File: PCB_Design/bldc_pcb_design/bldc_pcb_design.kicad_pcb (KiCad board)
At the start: 4 copper layers, 55.5 x 55.5 mm, 79 parts, among them IC1 DRV8305NPHPR, J1 Conn_01x06_Female, SW1 BOOT, SW2 RESET, U1 ESP32-WROOM-32D, U10 DS18S20Z+, U2 AS5600-ASOT, U3 LM2672M-3.3, U4 CSD18532NQ5BT, U5 CSD18532NQ5BT, U6 CSD18532NQ5BT, U7 CSD18532NQ5BT, U8 CSD18532NQ5BT, U9 CSD18532NQ5BT

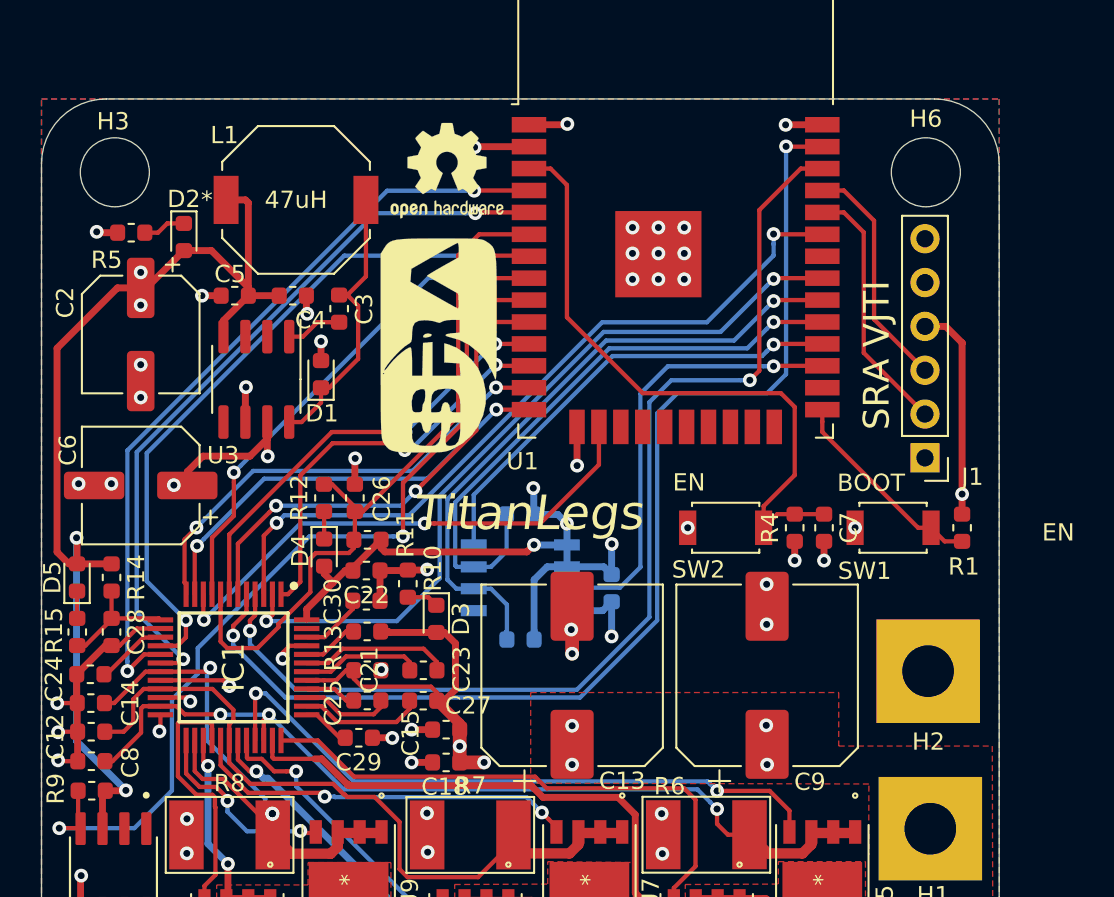
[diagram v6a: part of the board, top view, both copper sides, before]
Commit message: Routed buck converter LM2672 by copper fills - FCu
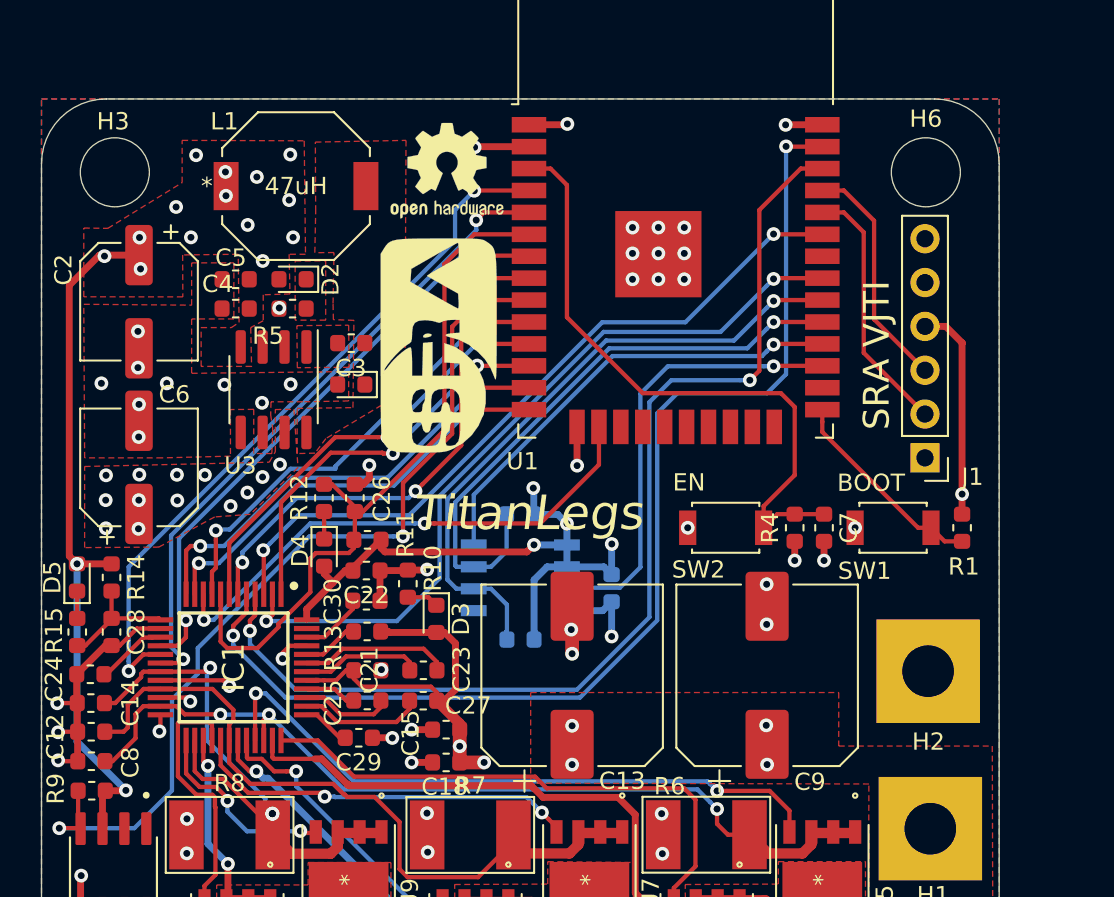
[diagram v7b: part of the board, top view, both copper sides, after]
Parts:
- moved R5 10.3 mm to (80.3, 73.9)
- moved D2 6.76 mm to (80.3, 72.2), turned to 180 degrees
- moved REF** 4.63 mm to (103.0, 104.5)
- moved C4 3.40 mm to (77.0, 73.9), turned to 180 degrees
- moved C3 2.12 mm to (83.7, 75.9), turned to 0 degrees
- moved C2 1.90 mm to (71.4, 73.5)
- moved D1 1.85 mm to (83.7, 78.3), turned to 180 degrees
- moved U3 1.17 mm to (79.2, 78.6)
- moved C6 1.05 mm to (71.4, 83.1), turned to 90 degrees
- moved C5 0.95 mm to (77.0, 72.2)
- moved L1 0.80 mm to (80.5, 66.8)
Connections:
- IC1 pad 17: ISENB -> POWER_IN
- U1 pad 4: ISENB -> POWER_IN
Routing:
- net ISENB: track 44.6 -> 0.00 mm, vias 2 -> 0
- net POWER_IN: track 54.2 -> 86.7 mm, vias 23 -> 36
- net 3V3_IN: track 114.9 -> 93.4 mm, vias 11 -> 23
- net Net-(C3-Pad2): track 16.4 -> 0.00 mm
- net GND: track 57.0 -> 50.7 mm, vias 55 -> 56
- net ISENA: track 40.2 -> 34.7 mm
- net ISENC: track 43.0 -> 37.7 mm
- net Net-(C3-Pad1): track 3.24 -> 0.00 mm
- net Net-(D2-Pad1): track 2.49 -> 0.00 mm
- net DRV_LA: track 43.7 -> 42.6 mm
- net DRV_EN_GATE: track 23.8 -> 23.1 mm
- net DRV_SPI_MISO: track 25.4 -> 24.7 mm
- net DRV_SPI_CLK: track 26.8 -> 26.3 mm
- added copper zone on F.Cu, net 3V3_IN
- added copper zone on F.Cu, net GND
- added copper zone on F.Cu, net Net-(C3-Pad1)
- added copper zone on F.Cu, net Net-(C3-Pad2)
- added copper zone on F.Cu, net Net-(D2-Pad1)

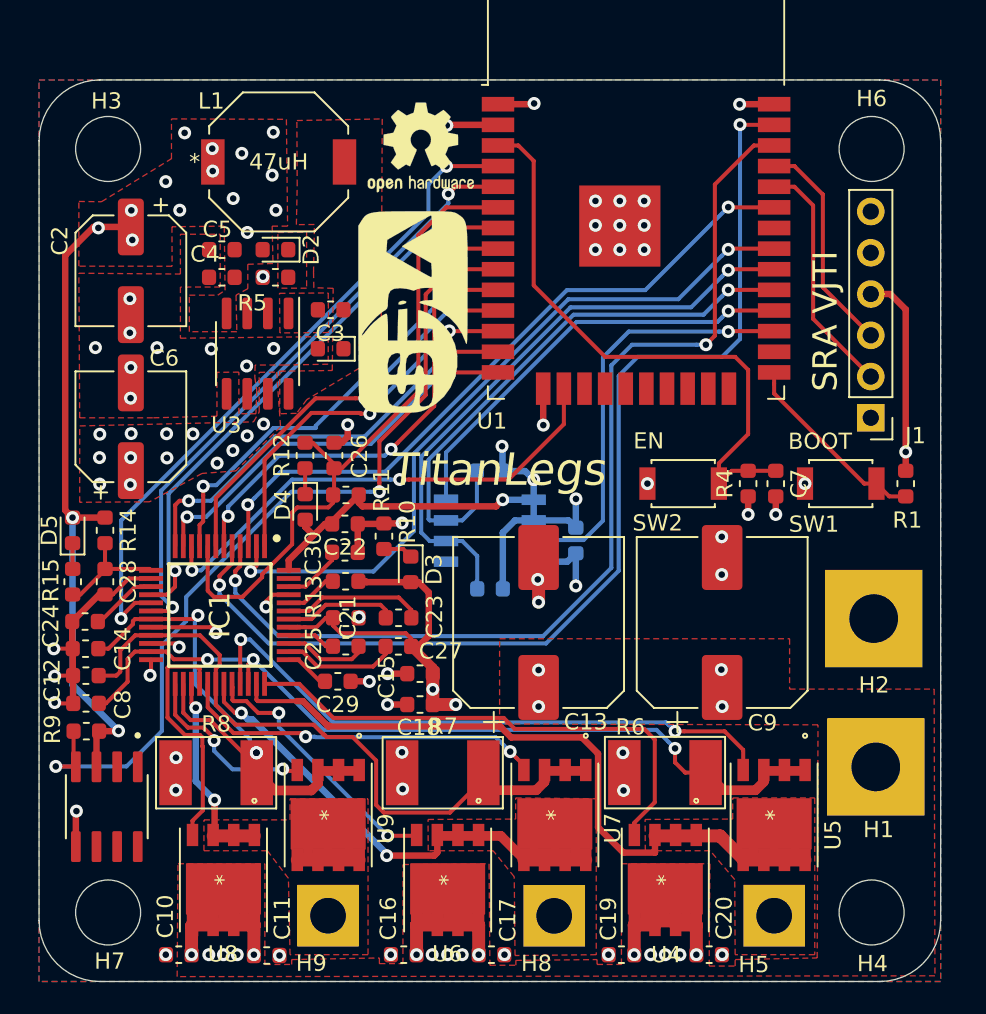
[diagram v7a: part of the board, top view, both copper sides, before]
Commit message: Re-routed DRV8305 using corrected underneath GND pad footprint, back mounted Temp sensor
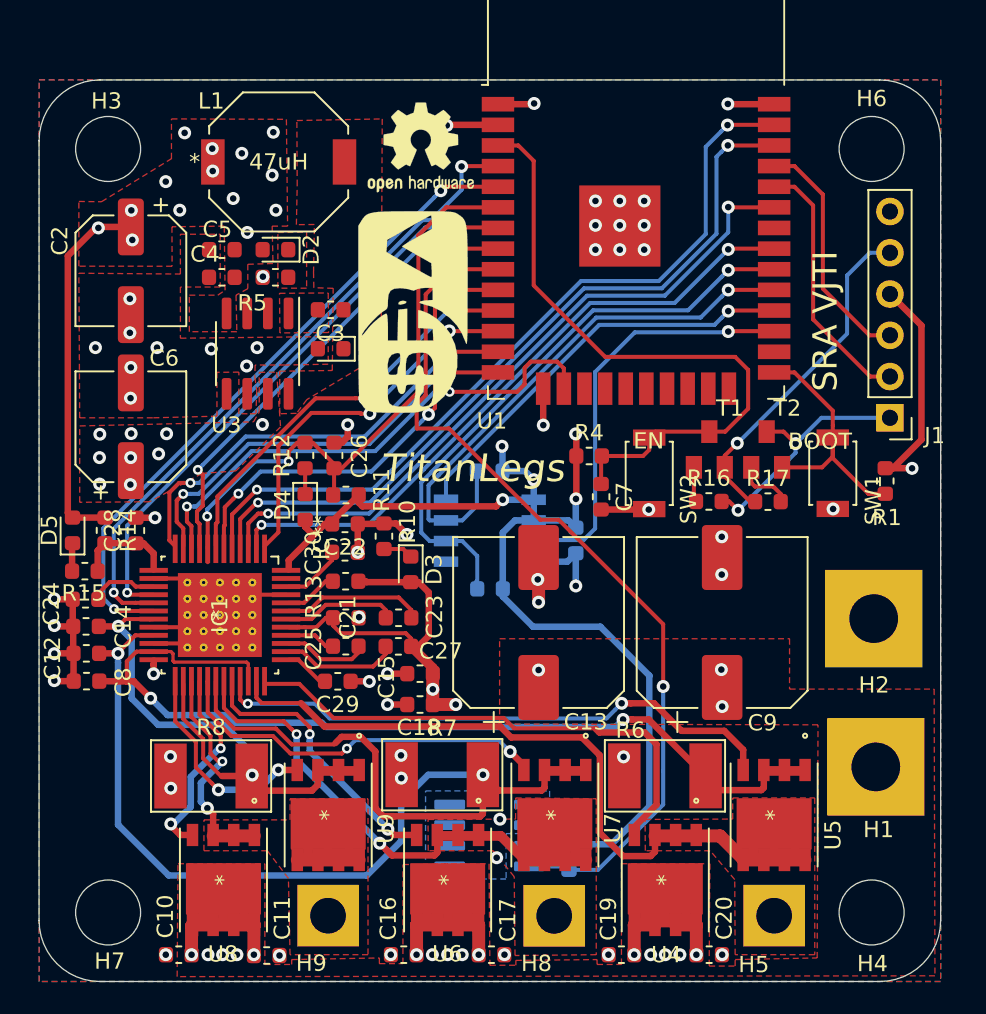
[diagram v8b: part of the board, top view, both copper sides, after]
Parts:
- added R16: 10k, Resistor_SMD:R_0603_1608Metric, F.Cu at (107.0, 87.7)
- added R17: 10k, Resistor_SMD:R_0603_1608Metric, F.Cu at (110.6, 87.7)
- added T1: BC847, BC847:BC847, F.Cu at (107.0, 84.5)
- added T2: BC847, BC847:BC847, F.Cu at (110.5, 84.5)
- IC1: footprint DRV8305NPHPR:DRV8305NPHPR -> DRV8305NPHPR:DRV8305NEPHPRQ1_with_GND_pads
- R9, U10: moved to B.Cu
- moved R9 30.7 mm to (98.4, 109.6), turned to 270 degrees
- moved U10 23.6 mm to (93.5, 108.3), turned to 180 degrees
- moved C7 10.8 mm to (100.3, 87.4)
- moved R4 9.94 mm to (99.6, 84.9), turned to 0 degrees
- moved REF** 4.22 mm to (103.2, 100.2)
- moved C28 3.68 mm to (71.7, 89.5), turned to 90 degrees
- moved G*** 2.56 mm to (78.7, 100.7)
- moved SW2 2.18 mm to (103.3, 86.0), turned to 90 degrees
- moved C12 1.37 mm to (68.7, 97.0)
- moved C14 1.37 mm to (68.6, 95.4)
- moved C24 1.37 mm to (68.6, 93.7)
- moved C8 1.37 mm to (68.7, 98.8)
- moved R1 1.27 mm to (117.8, 86.4)
- moved J1 1.18 mm to (118.1, 82.5)
- moved R15 0.99 mm to (68.6, 92.0), turned to 0 degrees
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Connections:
- IC1 pad 17: POWER_IN -> ISENB
- J1 pad 1: DTR -> ~DTR
- J1 pad 5: CTS -> ~RTS
- U1 pad 4: POWER_IN -> ISENB
- U10 pad 1: (no net) -> GND
- U10 pad 2: (no net) -> GND
- U10 pad 6: (no net) -> GND
- U10 pad 7: (no net) -> GND
- U10 pad 8: (no net) -> GND
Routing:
- net POWER_IN: track 86.7 -> 45.0 mm, vias 36 -> 29
- net ISENB: track 0.00 -> 40.4 mm, vias 0 -> 2
- net SLB: track 43.2 -> 75.8 mm, vias 0 -> 2
- net ~RTS: track 0.00 -> 21.2 mm, vias 0 -> 1
- net DRV_LB: track 66.7 -> 48.6 mm
- net DRV_HB: track 62.6 -> 47.0 mm
- net ~DTR: track 0.00 -> 15.4 mm, vias 0 -> 2
- net 3V3_IN: track 93.4 -> 108.1 mm, vias 23 -> 21
- net SLA: track 52.9 -> 58.4 mm, vias 3 -> 2
- net DRV_HA: track 45.0 -> 40.2 mm
- net Net-(R17-Pad2): track 0.00 -> 3.52 mm
- net BOOT: track 12.0 -> 15.5 mm
- net DRV_nFAULT: track 41.4 -> 38.1 mm, vias 0 -> 2
- net RESET: track 37.5 -> 40.7 mm
- net ISENC: track 37.7 -> 40.7 mm
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- added copper zone on B.Cu, net GND
